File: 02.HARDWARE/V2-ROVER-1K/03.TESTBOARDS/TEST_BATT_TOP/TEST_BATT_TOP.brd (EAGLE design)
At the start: 27 x 27 mm, 0 parts

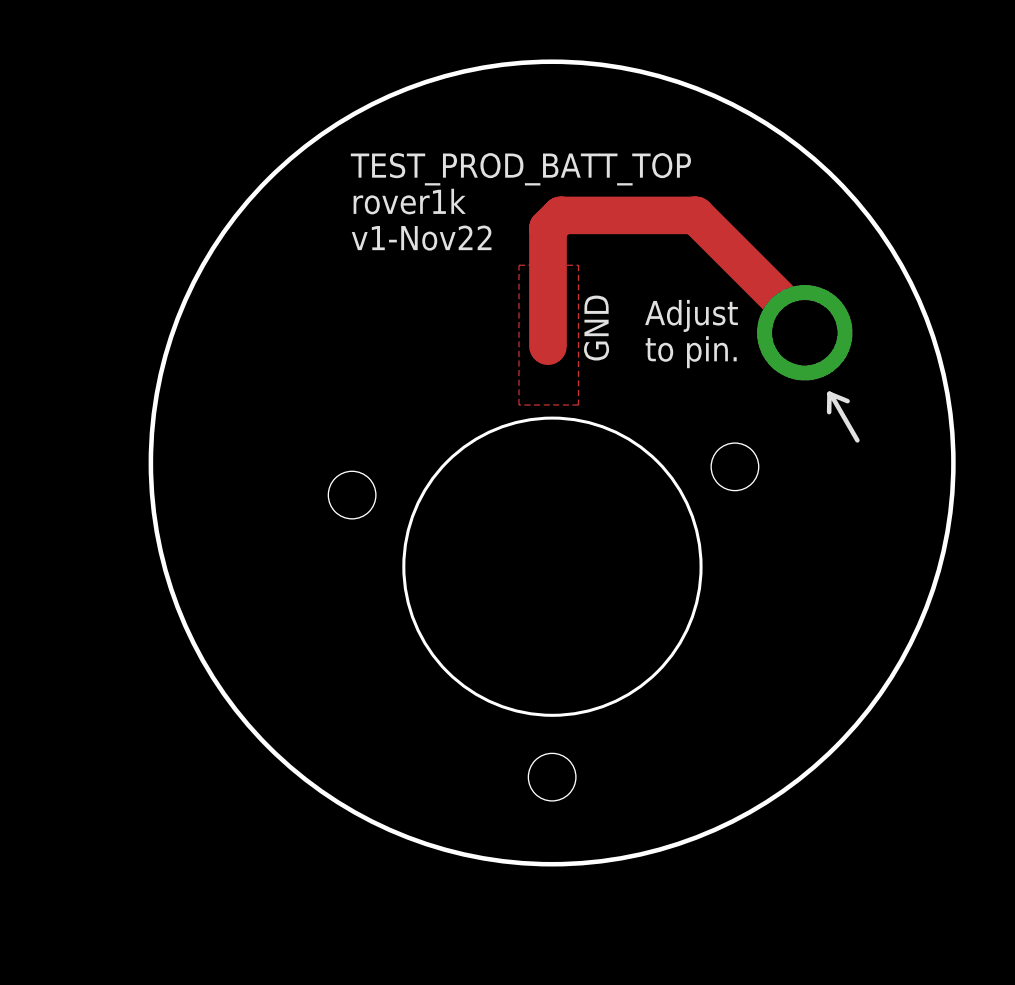
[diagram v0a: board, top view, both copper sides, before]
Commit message: Revisado y listo para pedido PCBWAY
Revision ultima antes de pedido de produccion
Modificacion de nombres
Cambio de directorio a TESTBOARDS
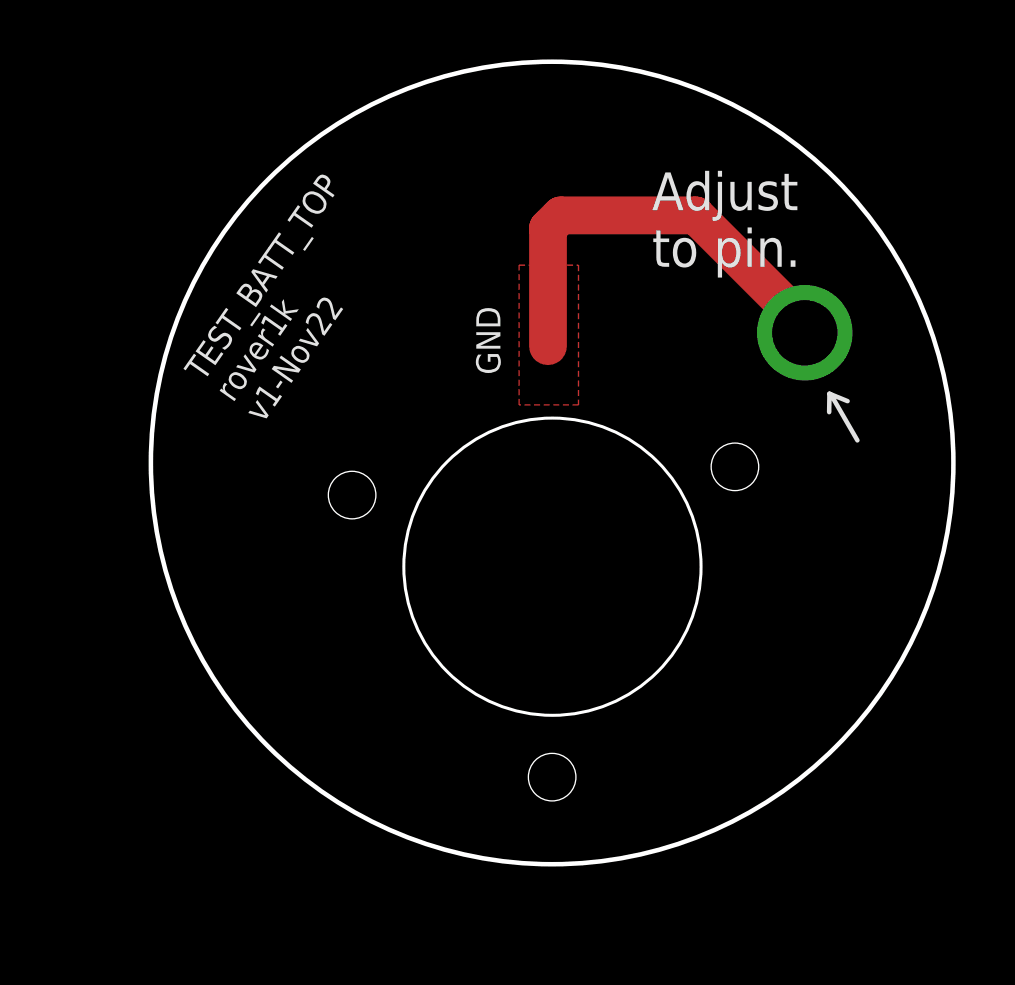
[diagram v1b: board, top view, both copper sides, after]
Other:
- board text added: "TEST_BATT_TOP rover1k v1-Nov22"
- board text removed: "TEST_PROD_BATT_TOP rover1k v1-Nov22"
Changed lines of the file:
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@@
 <layer number="2" name="Route2" color="16" fill="1" visible="no" active="no"/>
 <layer number="15" name="Route15" color="23" fill="1" visible="no" active="yes"/>
-<layer number="16" name="Bottom" color="1" fill="1" visible="no" active="yes"/>
+<layer number="16" name="Bottom" color="1" fill="1" visible="yes" active="yes"/>
 <layer number="17" name="Pads" color="2" fill="1" visible="yes" active="yes"/>
 <layer number="18" name="Vias" color="2" fill="1" visible="yes" active="yes"/>
@@
 <wire x1="53.66" y1="44.79" x2="53.65" y2="44.17" width="0.1524" layer="25"/>
 <wire x1="53.66" y1="44.79" x2="54.27" y2="44.54" width="0.1524" layer="25"/>
-<text x="47.45" y="45.88" size="0.8128" layer="25">Adjust
+<text x="47.69" y="49.06" size="1.27" layer="25">Adjust
 to pin.</text>
-<text x="37.56" y="49.62" size="0.8128" layer="25">TEST_PROD_BATT_TOP
+<text x="34.58906875" y="43.767046875" size="0.8128" layer="25" rot="R55">TEST_BATT_TOP
 rover1k
 v1-Nov22</text>
-<text x="46.23" y="45.85" size="0.8128" layer="25" rot="R90">GND</text>
+<text x="42.59" y="45.43" size="0.8128" layer="25" rot="R90">GND</text>
 </plain>
 <attributes>

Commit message: Cierre ISSUE #3
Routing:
- net N$1: track 0.00 -> 15.2 mm, vias 0 -> 2
- net GND: track 14.6 -> 0.00 mm, vias 1 -> 0
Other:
- board text added: "TEST_BATT_TOP rover1k v2-Nov22"
- board text removed: "TEST_BATT_TOP rover1k v1-Nov22"
